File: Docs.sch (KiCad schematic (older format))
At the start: 0 parts

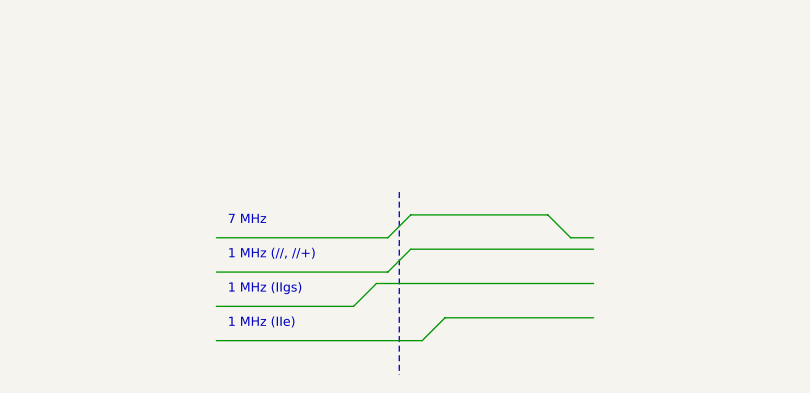
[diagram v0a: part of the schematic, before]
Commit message: added some disassembly of RamFactor
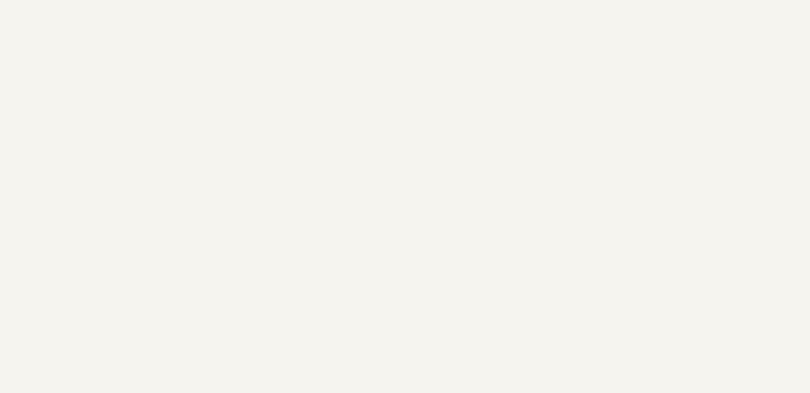
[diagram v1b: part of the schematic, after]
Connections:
- wire segments 297 -> 283
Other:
- note removed: "1 MHz (//, //+)"
- note removed: "1 MHz (IIe)"
- note removed: "1 MHz (IIgs)"
- note removed: "7 MHz"
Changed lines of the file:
@@
 Wire Wire Line
 	6150 1450 7300 1450
-Wire Wire Line
-	3550 6050 3450 6150
-Wire Wire Line
-	3300 6450 3400 6350
-Wire Wire Line
-	3600 6600 3700 6500
-Wire Notes Line
-	3500 5950 3500 6750
-Text Notes 2750 6100 0    40   ~ 0
-7 MHz
-Text Notes 2750 6400 0    40   ~ 0
-1 MHz (IIgs)
-Text Notes 2750 6550 0    40   ~ 0
-1 MHz (IIe)
-Wire Wire Line
-	3450 6300 3550 6200
-Text Notes 2750 6250 0    40   ~ 0
-1 MHz (//, //+)
-Wire Wire Line
-	2700 6450 3300 6450
-Wire Wire Line
-	2700 6600 3600 6600
-Wire Wire Line
-	4250 6150 4150 6050
-Wire Wire Line
-	3550 6050 4150 6050
-Wire Wire Line
-	3550 6200 4350 6200
-Wire Wire Line
-	4250 6150 4350 6150
-Wire Wire Line
-	3400 6350 4350 6350
-Wire Wire Line
-	3700 6500 4350 6500
-Wire Wire Line
-	2700 6300 3450 6300
-Wire Wire Line
-	2700 6150 3450 6150
 Connection ~ 1050 2800
 Wire Wire Line

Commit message: New schematic revision
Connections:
- wire segments 283 -> 245
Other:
- note added: "Information here may be out of date,\nsuperseded by ./cpld/GR8RAM.v"
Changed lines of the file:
@@
 Sheet 2 2
 Title "GR8RAM"
-Date "2019-07-23"
-Rev "0.1"
+Date "2019-10-13"
+Rev "0.9"
 Comp "Garrett's Workshop"
 Comment1 ""
@@
 D (wr)
 Wire Wire Line
-	4800 1900 4750 1950
-Wire Wire Line
-	4800 2000 4750 1950
-Wire Wire Line
-	4750 1950 1650 1950
-Wire Wire Line
 	4800 1900 6400 1900
 Wire Wire Line
@@
 Wire Wire Line
 	9600 2000 9550 1950
-Wire Wire Line
-	1600 1900 1650 1950
-Wire Wire Line
-	1600 2000 1650 1950
 Wire Wire Line
 	9600 1900 10400 1900
@@
 	1350 1450 1300 1550
 Wire Wire Line
-	4650 2600 5250 2600
-Wire Wire Line
-	9450 2600 10050 2600
-Wire Wire Line
-	4650 2750 4950 2750
-Wire Wire Line
-	9450 2750 9750 2750
-Wire Wire Line
 	2500 2350 2550 2450
 Wire Wire Line
 	2550 2450 3100 2450
 Wire Wire Line
-	4050 2900 4900 2900
-Wire Wire Line
 	10000 2900 10050 2800
 Wire Wire Line
@@
 Wire Wire Line
 	5200 2900 5250 2800
-Wire Wire Line
-	4050 2900 4000 2800
 Wire Wire Line
 	3400 2900 3450 2800
@@
 Text Notes 800  2900 2    50   ~ 0
 ~RAS~
-Wire Wire Line
-	900  2500 2250 2500
 Text Notes 7100 3800 0    50   ~ 0
 RA[10:8] = (RAMSEL & (S4 | S5)) ? Addr[10:8] : Addr[21:19] @ C7M\nRA[7:1] = RAMSEL ? (S4 ? Addr[7:1] : Addr[18:12]) : Bank[6:0] @ C7M\nRA[0] = RAMSEL ? (S4 ? Addr[0] : Addr[11]) : A[11] @ C7M
-Wire Wire Line
-	8850 2900 9700 2900
 Text Notes 3700 4850 0    50   ~ 0
 DBEN = ~S2~ & ~S3~ @ C7M\nRCS = IOSEL  | (IOSTRB & IOROMEN)\nROE = R~W~\nRWE = ~R~W & (DEVSEL | IOSEL | IOSTRB)\n\nCASr = (S1 & Ref[3:0]==0) | (S5 & RAMSEL) @ C7M\nCASf = ((S5 & R~W~) | S6 | S7) & RAMSEL @ ~C7M~\n\nRASf = (S4 & RAMSEL) | (S5 & RAMSEL & ~R~W) | (S2 & Ref[3:0]==0) @ ~C7M~\nCAS0 = CASr | (CASf & DEVSEL & ~Addr[22]~)\nCAS1 = CASr | (CASf & DEVSEL & Addr[22])
@@
 	9700 2900 9750 2800
 Wire Wire Line
-	900  2350 2500 2350
-Wire Wire Line
-	900  2650 1350 2650
-Wire Wire Line
-	900  2800 1050 2800
-Wire Wire Line
 	900  1550 1300 1550
 Wire Wire Line
@@
 	6350 1550 6400 1450
 Wire Wire Line
-	3450 1550 6100 1550
-Wire Wire Line
-	6100 1550 6350 1550
-Wire Wire Line
 	6150 1450 7300 1450
-Connection ~ 1050 2800
-Wire Wire Line
-	1050 2800 2800 2800
-Connection ~ 1350 2650
-Wire Wire Line
-	1350 2650 2500 2650
-Connection ~ 1650 1950
-Connection ~ 1650 2100
-Connection ~ 2250 2500
-Wire Wire Line
-	2250 2500 4600 2500
-Connection ~ 2500 2350
-Wire Wire Line
-	2500 2350 3150 2350
-Connection ~ 2500 2650
-Wire Wire Line
-	2500 2650 3150 2650
-Connection ~ 2800 2800
-Wire Wire Line
-	2800 2800 3450 2800
-Connection ~ 3150 2350
-Wire Wire Line
-	3150 2350 4900 2350
-Connection ~ 3150 2650
-Wire Wire Line
-	3150 2650 4600 2650
-Connection ~ 3450 2800
-Wire Wire Line
-	3450 2800 4000 2800
-Connection ~ 4000 2800
-Wire Wire Line
-	4000 2800 4950 2800
-Connection ~ 4600 2500
-Wire Wire Line
-	4600 2500 5200 2500
-Connection ~ 4600 2650
-Wire Wire Line
-	4600 2650 4900 2650
-Connection ~ 4750 1950
-Connection ~ 4900 2350
-Wire Wire Line
-	4900 2350 5550 2350
-Connection ~ 4900 2650
-Wire Wire Line
-	4900 2650 6150 2650
-Connection ~ 4900 2900
-Wire Wire Line
-	4900 2900 5200 2900
-Connection ~ 4950 2750
-Wire Wire Line
-	4950 2750 6100 2750
-Connection ~ 4950 2800
-Wire Wire Line
-	4950 2800 5250 2800
-Connection ~ 5000 2100
-Connection ~ 5200 2500
-Wire Wire Line
-	5200 2500 6450 2500
-Connection ~ 5250 2600
-Wire Wire Line
-	5250 2600 6400 2600
-Connection ~ 5250 2800
-Wire Wire Line
-	5250 2800 7600 2800
-Connection ~ 5550 2350
-Wire Wire Line
-	5550 2350 7300 2350
-Connection ~ 6100 1550
 Wire Bus Line
 	6100 1550 6100 2250
-Connection ~ 6150 2650
-Wire Wire Line
-	6150 2650 7300 2650
-Connection ~ 6450 1950
-Connection ~ 6450 2100
-Connection ~ 6450 2500
-Wire Wire Line
-	6450 2500 9400 2500
-Connection ~ 7300 2350
-Wire Wire Line
-	7300 2350 7950 2350
-Connection ~ 7300 2650
-Wire Wire Line
-	7300 2650 7950 2650
-Connection ~ 7600 2800
-Wire Wire Line
-	7600 2800 8250 2800
-Connection ~ 7950 2350
-Wire Wire Line
-	7950 2350 9700 2350
-Connection ~ 7950 2650
-Wire Wire Line
-	7950 2650 9400 2650
-Connection ~ 8250 2800
-Wire Wire Line
-	8250 2800 8800 2800
-Connection ~ 8800 2800
-Wire Wire Line
-	8800 2800 9750 2800
-Connection ~ 9400 2500
-Wire Wire Line
-	9400 2500 10000 2500
-Connection ~ 9400 2650
-Wire Wire Line
-	9400 2650 9700 2650
-Connection ~ 9550 1950
-Connection ~ 9700 2350
-Wire Wire Line
-	9700 2350 10350 2350
-Connection ~ 9700 2650
-Wire Wire Line
-	9700 2650 10350 2650
-Connection ~ 9700 2900
-Wire Wire Line
-	9700 2900 10000 2900
-Connection ~ 9750 2750
-Wire Wire Line
-	9750 2750 10300 2750
-Connection ~ 9750 2800
-Wire Wire Line
-	9750 2800 10050 2800
-Connection ~ 9800 2100
-Connection ~ 10000 2500
-Wire Wire Line
-	10000 2500 10400 2500
-Connection ~ 10050 2600
-Wire Wire Line
-	10050 2600 10400 2600
-Connection ~ 10050 2800
-Wire Wire Line
-	10050 2800 10400 2800
-Connection ~ 10350 2350
-Wire Wire Line
-	10350 2350 10400 2350
-Connection ~ 10350 2650
-Wire Wire Line
-	10350 2650 10400 2650
 Wire Wire Line
 	1350 1450 3400 1450
@@
 	6600 1600 6650 1700
 Wire Wire Line
-	3450 1600 6150 1600
-Wire Wire Line
 	6150 1600 6200 1700
 Wire Wire Line
-	6200 1700 6650 1700
-Wire Wire Line
 	3400 1700 1350 1700
 Wire Wire Line
@@
 	900  1600 1300 1600
 Wire Wire Line
-	6650 1700 8200 1700
-Connection ~ 6650 1700
-Wire Wire Line
 	8200 1700 8250 1600
 Wire Wire Line
 	8250 1600 10300 1600
-Connection ~ 6150 1600
-Wire Wire Line
-	6150 1600 6600 1600
 Wire Wire Line
 	10400 1650 10450 1650
@@
 Text Notes 6300 1100 0    40   ~ 0
 S7
+Text Notes 1200 6100 0    200  ~ 0
+Information here may be out of date,\nsuperseded by ./cpld/GR8RAM.v
+Wire Wire Line
+	1600 2000 1650 1950
+Wire Wire Line
+	1600 1900 1650 1950
+Wire Wire Line
+	4750 1950 1650 1950
+Wire Wire Line
+	4800 2000 4750 1950
+Wire Wire Line
+	4800 1900 4750 1950
+Wire Wire Line
+	3450 1550 6350 1550
+Wire Wire Line
+	3450 1600 6600 1600
+Wire Wire Line
+	6200 1700 8200 1700
+Wire Wire Line
+	9450 2600 10400 2600
+Wire Wire Line
+	4650 2600 6400 2600
+Wire Wire Line
+	900  2500 10400 2500
+Wire Wire Line
+	4050 2900 4000 2800
+Wire Wire Line
+	1350 2650 2500 2650
+Wire Wire Line
+	4000 2800 3450 2800
+Wire Wire Line
+	2800 2800 1050 2800
+Wire Wire Line
+	4650 2750 6100 2750
+Wire Wire Line
+	4050 2900 5200 2900
+Wire Wire Line
+	4950 2800 7600 2800
+Wire Wire Line
+	3150 2650 7300 2650
+Wire Wire Line
+	9450 2750 10300 2750
+Wire Wire Line
+	8850 2900 10000 2900
+Wire Wire Line
+	7950 2650 10400 2650
+Wire Wire Line
+	8250 2800 10400 2800
+Wire Wire Line
+	900  2350 2500 2350
+Wire Wire Line
+	7950 2350 10400 2350
+Wire Wire Line
+	3150 2350 7300 2350
 $EndSCHEMATC

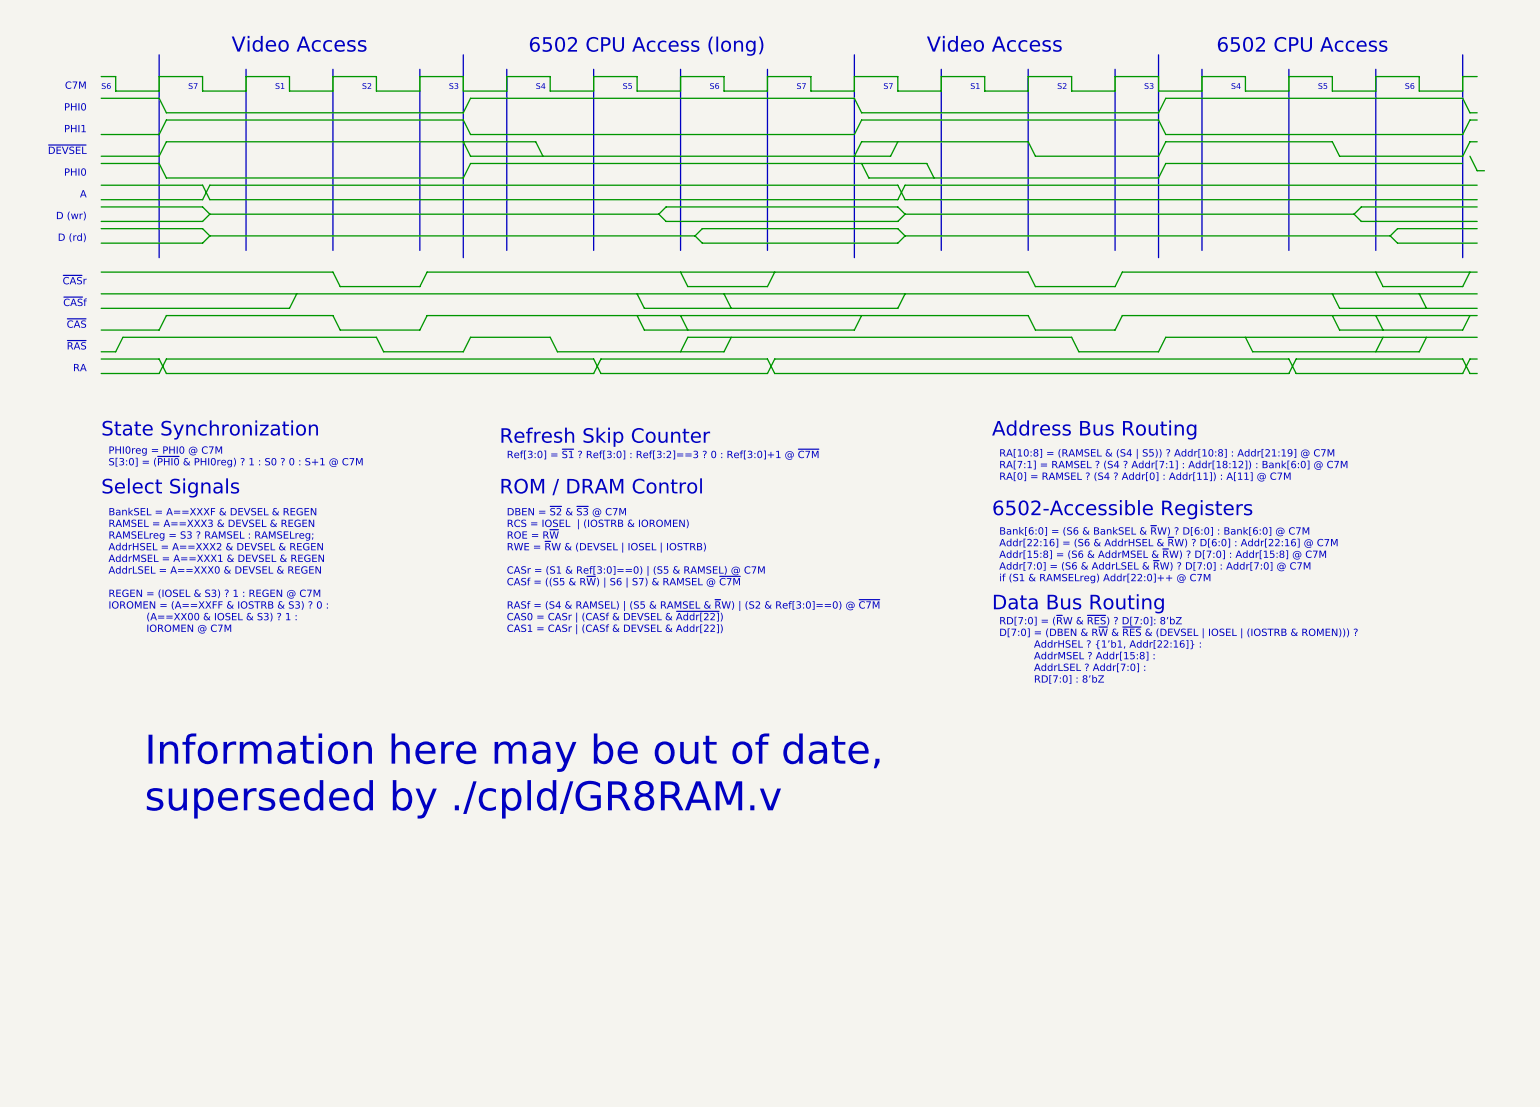
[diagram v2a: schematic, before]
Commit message: New PLD revision
For write operations, register data is latched and CAS signal becomes in the middle of S6, 70ns before the end of PHI0. This gives more write data setup time, which may be needed on the Apple II with the 1 MHz 6502.
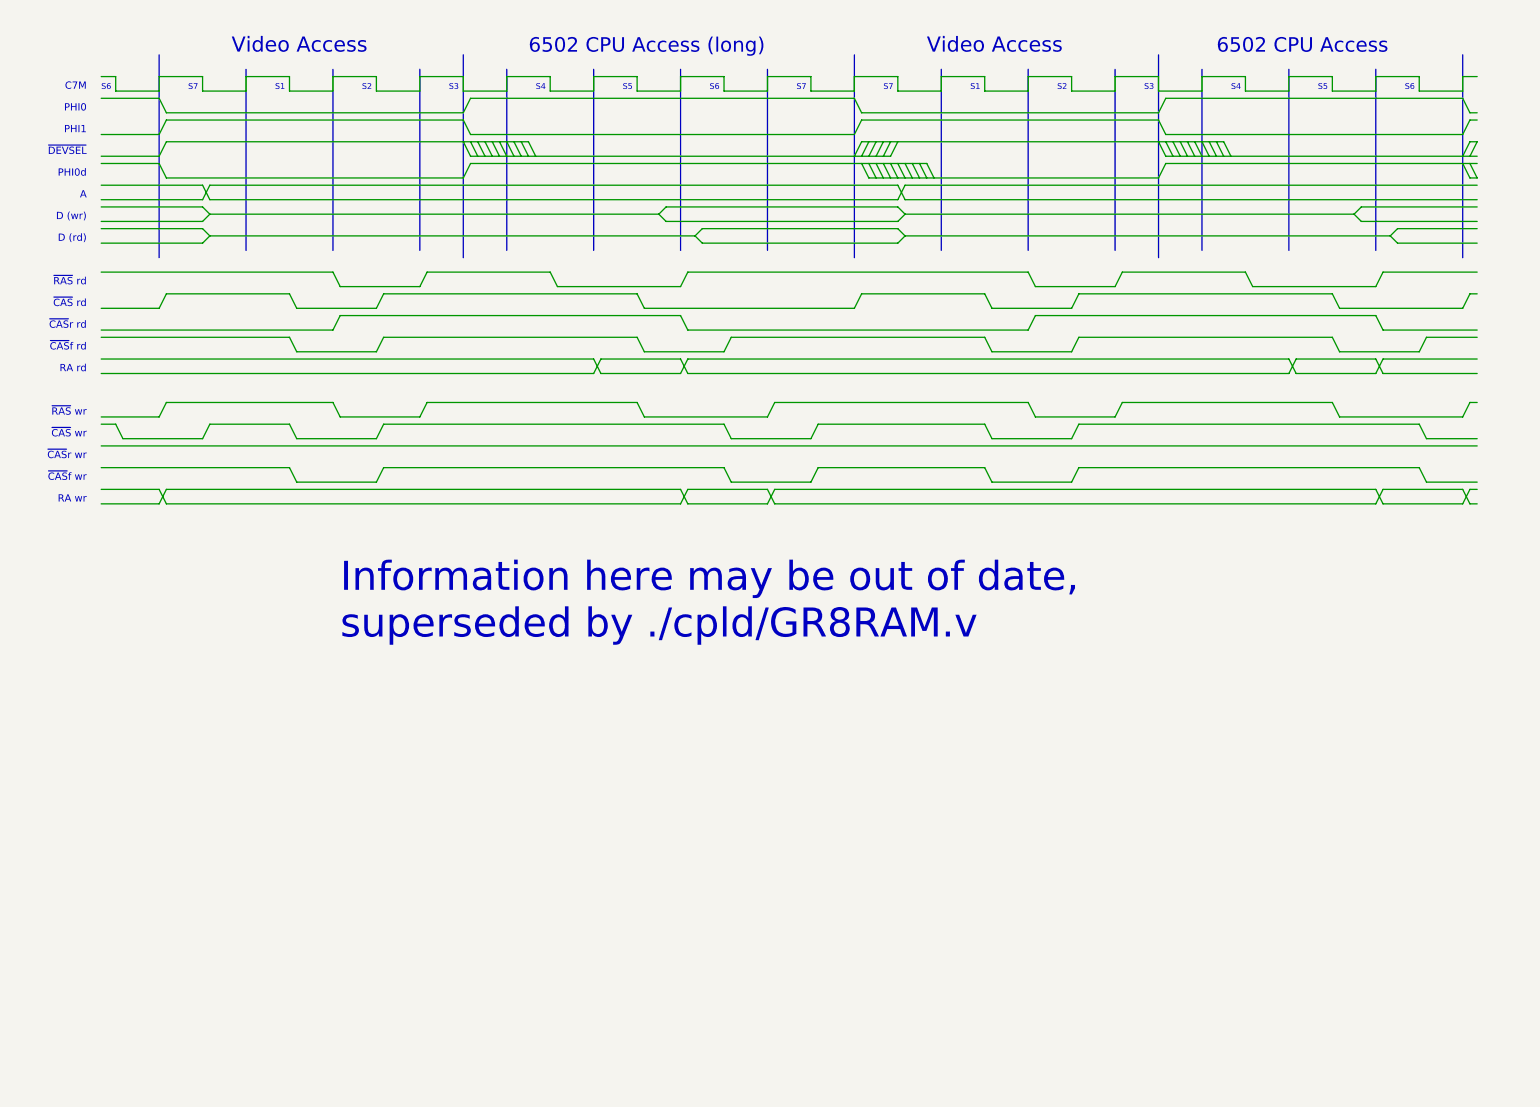
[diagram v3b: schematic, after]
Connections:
- wire segments 245 -> 343
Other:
- note added: "PHI0d"
- note added: "RA rd"
- note added: "RA wr"
- note added: "~CAS~ rd"
- note added: "~CAS~ wr"
- note added: "~CAS~f rd"
- note added: "~CAS~f wr"
- note added: "~CAS~r rd"
- note added: "~CAS~r wr"
- note added: "~RAS~ rd"
- note added: "~RAS~ wr"
- note removed: "6502-Accessible Registers"
- note removed: "Address Bus Routing"
- note removed: "BankSEL = A==XXXF & DEVSEL & REGEN\nRAMSEL = A==XXX3 & DEVSEL & REGEN\nRAMSELreg = S3 ? RAMSEL : RAMSELreg;\nAddrHSEL = A==XXX2 & DEVSEL & REGEN\nAddrMSEL = A==XXX1 & DEVSEL & REGEN\nAddrLSEL = A==XXX0 & DEVSEL & REGEN\n\nREGEN = (IOSEL & S3) ? 1 : REGEN @ C7M\nIOROMEN = (A==XXFF & IOSTRB & S3) ? 0 :\n (A==XX00 & IOSEL & S3) ? 1 :\n IOROMEN @ C7M"
- note removed: "Bank[6:0] = (S6 & BankSEL & ~R~W) ? D[6:0] : Bank[6:0] @ C7M\nAddr[22:16] = (S6 & AddrHSEL & ~R~W) ? D[6:0] : Addr[22:16] @ C7M\nAddr[15:8] = (S6 & AddrMSEL & ~R~W) ? D[7:0] : Addr[15:8] @ C7M\nAddr[7:0] = (S6 & AddrLSEL & ~R~W) ? D[7:0] : Addr[7:0] @ C7M\nif (S1 & RAMSELreg) Addr[22:0]++ @ C7M"
- note removed: "DBEN = ~S2~ & ~S3~ @ C7M\nRCS = IOSEL | (IOSTRB & IOROMEN)\nROE = R~W~\nRWE = ~R~W & (DEVSEL | IOSEL | IOSTRB)\n\nCASr = (S1 & Ref[3:0]==0) | (S5 & RAMSEL) @ C7M\nCASf = ((S5 & R~W~) | S6 | S7) & RAMSEL @ ~C7M~\n\nRASf = (S4 & RAMSEL) | (S5 & RAMSEL & ~R~W) | (S2 & Ref[3:0]==0) @ ~C7M~\nCAS0 = CASr | (CASf & DEVSEL & ~Addr[22]~)\nCAS1 = CASr | (CASf & DEVSEL & Addr[22])"
- note removed: "Data Bus Routing"
- note removed: "PHI0reg = PHI0 @ C7M\nS[3:0] = (~PHI0~ & PHI0reg) ? 1 : S0 ? 0 : S+1 @ C7M"
- note removed: "RA"
- note removed: "RA[10:8] = (RAMSEL & (S4 | S5)) ? Addr[10:8] : Addr[21:19] @ C7M\nRA[7:1] = RAMSEL ? (S4 ? Addr[7:1] : Addr[18:12]) : Bank[6:0] @ C7M\nRA[0] = RAMSEL ? (S4 ? Addr[0] : Addr[11]) : A[11] @ C7M"
- note removed: "RD[7:0] = (~R~W & ~RES~) ? D[7:0]: 8’bZ\nD[7:0] = (DBEN & R~W~ & ~RES~ & (DEVSEL | IOSEL | (IOSTRB & ROMEN))) ?\n AddrHSEL ? {1’b1, Addr[22:16]} : \n AddrMSEL ? Addr[15:8] : \n AddrLSEL ? Addr[7:0] : \n RD[7:0] : 8’bZ"
- note removed: "ROM / DRAM Control"
- note removed: "Ref[3:0] = ~S1~ ? Ref[3:0] : Ref[3:2]==3 ? 0 : Ref[3:0]+1 @ ~C7M~"
- note removed: "Refresh Skip Counter"
- note removed: "Select Signals"
- note removed: "State Synchronization"
- note removed: "~CAS~"
- note removed: "~CAS~f"
- note removed: "~CAS~r"
- note removed: "~RAS~"

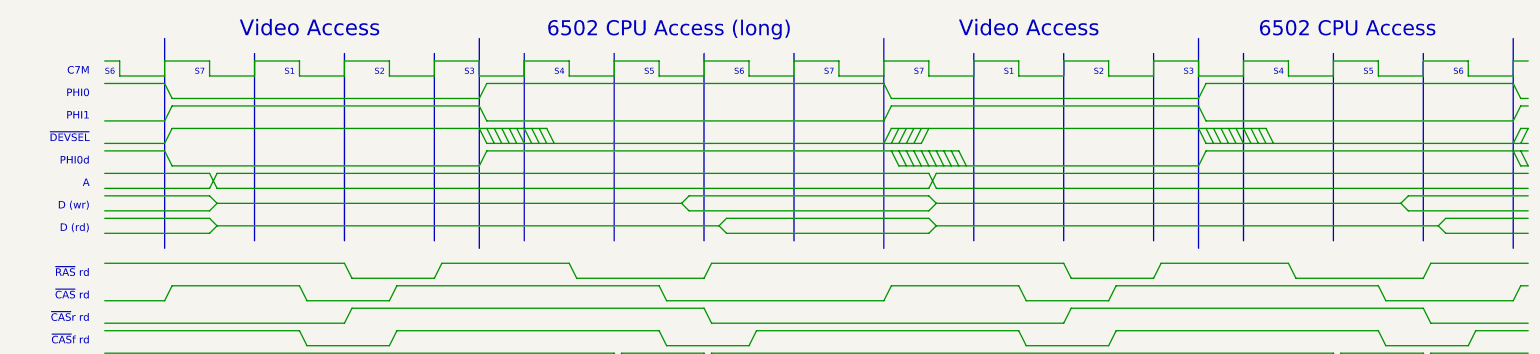
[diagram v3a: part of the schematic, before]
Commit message: Separated CSDBEN
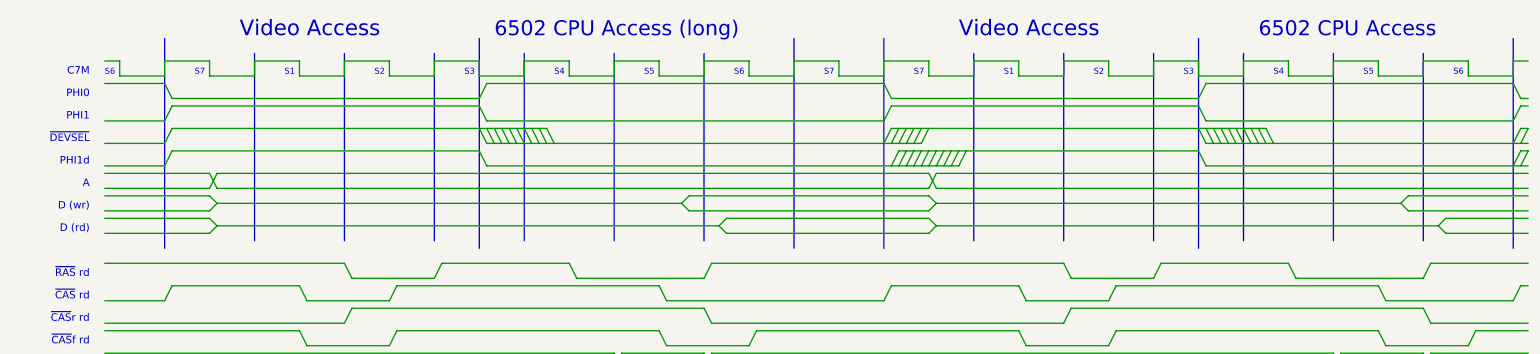
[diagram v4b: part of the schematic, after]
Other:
- note added: "PHI1d"
- note removed: "PHI0d"

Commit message: Board done?
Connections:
- wire segments 343 -> 1150
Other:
- note added: "ACT"
- note added: "AREF"
- note added: "C25M"
- note added: "CKE"
- note added: "CMD"
- note added: "MD"
- note added: "NOP"
- note added: "RD"
- note added: "SD"
- note added: "WR"
- note added: "~DEVSEL~r0"
- note removed: "6502 CPU Access"
- note removed: "6502 CPU Access (long)"
- note removed: "A"
- note removed: "C7M"
- note removed: "D (rd)"
- note removed: "D (wr)"
- note removed: "PHI1"
- note removed: "PHI1d"
- note removed: "RA rd"
- note removed: "RA wr"
- note removed: "S1"
- note removed: "S2"
- note removed: "S3"
- note removed: "S4"
- note removed: "S5"
- note removed: "S6"
- note removed: "S7"
- note removed: "Video Access"
- note removed: "~CAS~ rd"
- note removed: "~CAS~ wr"
- note removed: "~CAS~f rd"
- note removed: "~CAS~f wr"
- note removed: "~CAS~r rd"
- note removed: "~CAS~r wr"
- note removed: "~RAS~ rd"
- note removed: "~RAS~ wr"

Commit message: Fabbed
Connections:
- wire segments 1150 -> 580
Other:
- note added: "0"
- note added: "1"
- note added: "2"
- note added: "3"
- note added: "4"
- note added: "5"
- note added: "6"
- note added: "7"
- note added: "CKE (idle,rd)"
- note added: "CKE (idle,wr)"
- note added: "CKE (rd)"
- note added: "CKE (wr)"
- note added: "CMD (idle)"
- note added: "CMD (rd)"
- note added: "CMD (wr)"
- note added: "DEVSELr1\n"
- note added: "DEVSELr2"
- note added: "PD"
- note added: "PHI0r1"
- note added: "PHI0r2"
- note added: "PHI0r3"
- note added: "PHI0r4"
- note added: "ROMSPC <= A[15:12]==4’hC && A[11:8]!=4’h0 (use ROMSPCr2)\nRAMSPC <= A[15:12]==4’hC && A[11:8]==4’h0 && A[7] && A[7:0]!=4’h8 (use RAMSPCr2)"
- note added: "S"
- note removed: "CKE"
- note removed: "CMD"
- note removed: "~DEVSEL~r0"

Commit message: idk
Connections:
- wire segments 580 -> 568
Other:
- note added: "8"
- note added: "9"
- note added: "CKE (idle)"
- note removed: "CKE (idle,rd)"
- note removed: "CKE (idle,wr)"
- note removed: "PHI0r4"
